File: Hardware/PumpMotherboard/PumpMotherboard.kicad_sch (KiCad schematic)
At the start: 22 parts, among them J1 BTB, J2 AC_LEDs, J401 12V Input, J6 SW_IN0, J7 SW_IN1, J8 SW_IN2, Q10 MMBT3904, Q9 AO4407A, U2 AP63205WU

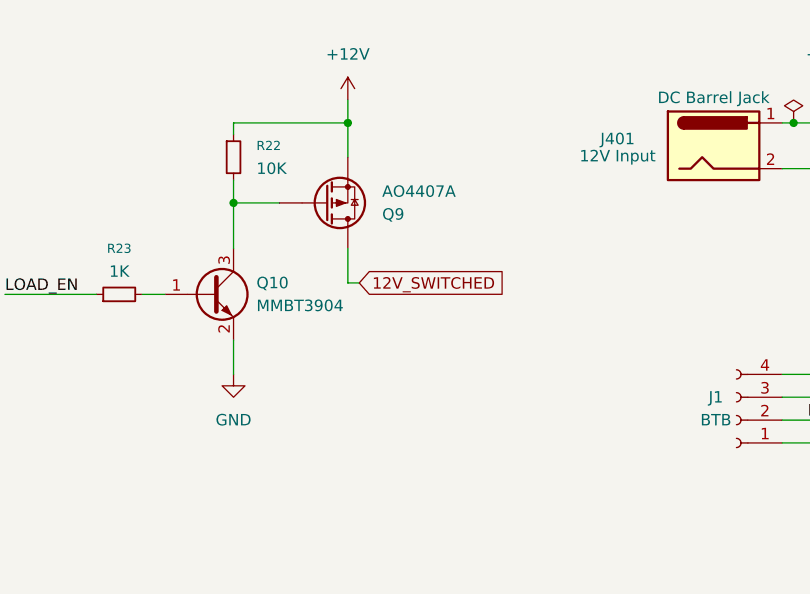
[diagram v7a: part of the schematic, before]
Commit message: Add flyback protection
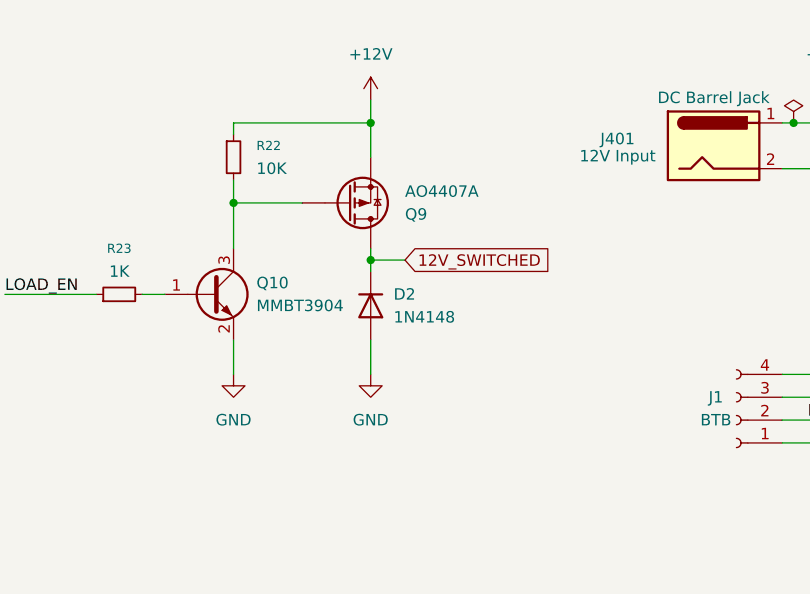
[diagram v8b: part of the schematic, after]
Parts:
- added D2: 1N4148, Diode_THT:D_DO-35_SOD27_P7.62mm_Horizontal, symbol Diode:1N4148
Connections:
- net 12V_SWITCHED: now also D2.1 (K)
- net GND: now also D2.2 (A)
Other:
- moved on the sheet: Q9
